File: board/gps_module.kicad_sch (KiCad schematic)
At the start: 0 parts

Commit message: Hopefully finished schema for pcb
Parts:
- added C11: 8.2p, symbol Device:C
- added C12, C9: 100n, symbol Device:C
- added C13: 4.7p, symbol Device:C
- added D4: LED, symbol Device:LED
- added J1: Conn_01x01_Pin, symbol Connector:Conn_01x01_Pin
- added L2, L3: 27n, symbol Device:L
- added R23: 10, symbol Device:R
- added R26: 470, symbol Device:R
- added TVS1: SMAJ30CA, Diode_SMD:D_SMA, symbol Diode:SMAJ30CA
- added U6: NEO-M7N, RF_GPS:ublox_NEO, symbol RF_GPS:NEO-M8N
- added U7: MAX2679B, Package_BGA:WLP-4_0.83x0.83mm_P0.4mm, symbol RF_Amplifier:MAX2679B
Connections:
- new net: C13.2, J1.1 (Pin_1), TVS1.2 (A2)
- new net: C13.1, L3.2
- new net: C11.2, U7.A2
- new net: D4.1 (K), R26.2
- new net: L3.1, U7.B1
- new net: L2.1, R23.2
- new net: R26.1, U6.3 (TIMEPULSE)
- new net +3V3: C12.2, C9.2, D4.2 (A), U6.23 (VCC), U7.A1 (Vcc)
- new net 3V3: U6.2 (D_SEL)
- new net GND: C12.1, C9.1, TVS1.1 (A1), U6.10 (GND), U6.12 (GND), U6.13 (GND), U6.24 (GND), U7.B2 (G)
- new net RF_IN: C11.1, L2.2, U6.11 (RF_IN)
- new net RX: U6.21 (RXD/SPI_MOSI)
- new net SDA_GPS: U6.18 (SDA/~{SPI_CS})
- new net SLC_GPS: U6.19 (SCL/SPI_CLK)
- new net TX: U6.20 (TXD/SPI_MISO)
- new net VCC_RF: R23.1, U6.8 (~{RESET}), U6.9 (VCC_RF)
- no-connect marks 0 -> 7
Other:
- note added: "GPS signal amplification"
- note added: "uBlox NEO M7N module"

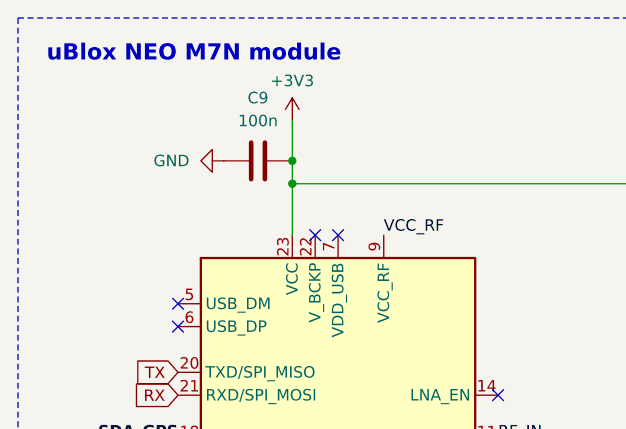
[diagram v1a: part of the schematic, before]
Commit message: Minor changes in shchema for PCB
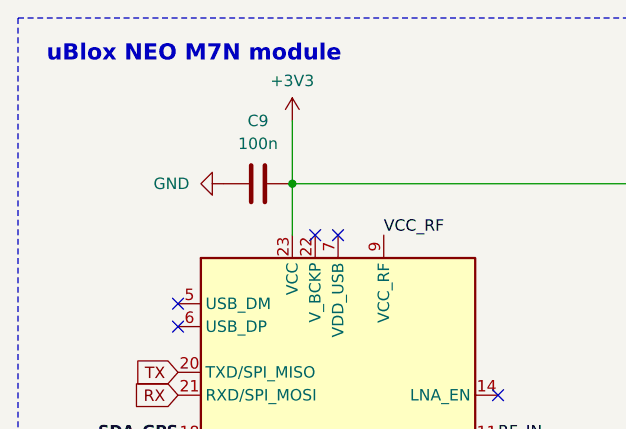
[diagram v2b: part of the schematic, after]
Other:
- moved on the sheet: C9
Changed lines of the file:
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@@
 (kicad_sch (version 20230121) (generator eeschema)
   (paper "A4")
-  (junction (at 94.615 73.66) (diameter 0) (color 0 0 0 0)
-  )
   (junction (at 221.615 95.885) (diameter 0) (color 0 0 0 0)
   )
@@
     (stroke (width 0) (type default))
   )
-  (wire (pts (xy 94.615 73.66) (xy 94.615 76.2))
-    (stroke (width 0) (type default))
-  )
   (wire (pts (xy 221.615 95.885) (xy 224.79 95.885))
     (stroke (width 0) (type default))
@@
     (stroke (width 0) (type default))
   )
-  (wire (pts (xy 94.615 69.215) (xy 94.615 73.66))
+  (wire (pts (xy 94.615 69.215) (xy 94.615 76.2))
     (stroke (width 0) (type default))
   )
@@
     )
   )
-  (symbol (lib_id "power:GND") (at 86.995 73.66 270) (unit 1)
-    (in_bom yes) (on_board yes) (dnp no) (fields_autoplaced)
-    (property "Reference" "#PWR041" (at 80.645 73.66 0)
-      (effects (font (size 1.27 1.27)) hide)
-    )
-    (property "Value" "GND" (at 83.185 73.66 90)
+  (symbol (lib_id "power:GND") (at 86.995 76.2 270) (unit 1)
+    (in_bom yes) (on_board yes) (dnp no) (fields_autoplaced)
+    (property "Reference" "#PWR041" (at 80.645 76.2 0)
+      (effects (font (size 1.27 1.27)) hide)
+    )
+    (property "Value" "GND" (at 83.185 76.2 90)
       (effects (font (size 1.27 1.27)) (justify right))
     )
-    (property "Footprint" "" (at 86.995 73.66 0)
-      (effects (font (size 1.27 1.27)) hide)
-    )
-    (property "Datasheet" "" (at 86.995 73.66 0)
+    (property "Footprint" "" (at 86.995 76.2 0)
+      (effects (font (size 1.27 1.27)) hide)
+    )
+    (property "Datasheet" "" (at 86.995 76.2 0)
       (effects (font (size 1.27 1.27)) hide)
     )
@@
     )
   )
-  (symbol (lib_id "Device:C") (at 90.805 73.66 90) (unit 1)
-    (in_bom yes) (on_board yes) (dnp no) (fields_autoplaced)
-    (property "Reference" "C9" (at 90.805 66.675 90)
-      (effects (font (size 1.27 1.27)))
-    )
-    (property "Value" "100n" (at 90.805 69.215 90)
-      (effects (font (size 1.27 1.27)))
-    )
-    (property "Footprint" "" (at 94.615 72.6948 0)
-      (effects (font (size 1.27 1.27)) hide)
-    )
-    (property "Datasheet" "~" (at 90.805 73.66 0)
-      (effects (font (size 1.27 1.27)) hide)
-    )
+  (symbol (lib_id "Device:C") (at 90.805 76.2 90) (unit 1)
+    (in_bom yes) (on_board yes) (dnp no) (fields_autoplaced)
+    (property "Reference" "C9" (at 90.805 69.215 90)
+      (effects (font (size 1.27 1.27)))
+    )
+    (property "Value" "100n" (at 90.805 71.755 90)
+      (effects (font (size 1.27 1.27)))
+    )
+    (property "Footprint" "" (at 94.615 75.2348 0)
+      (effects (font (size 1.27 1.27)) hide)
+    )
+    (property "Datasheet" "~" (at 90.805 76.2 0)
+      (effects (font (size 1.27 1.27)) hide)
+    )

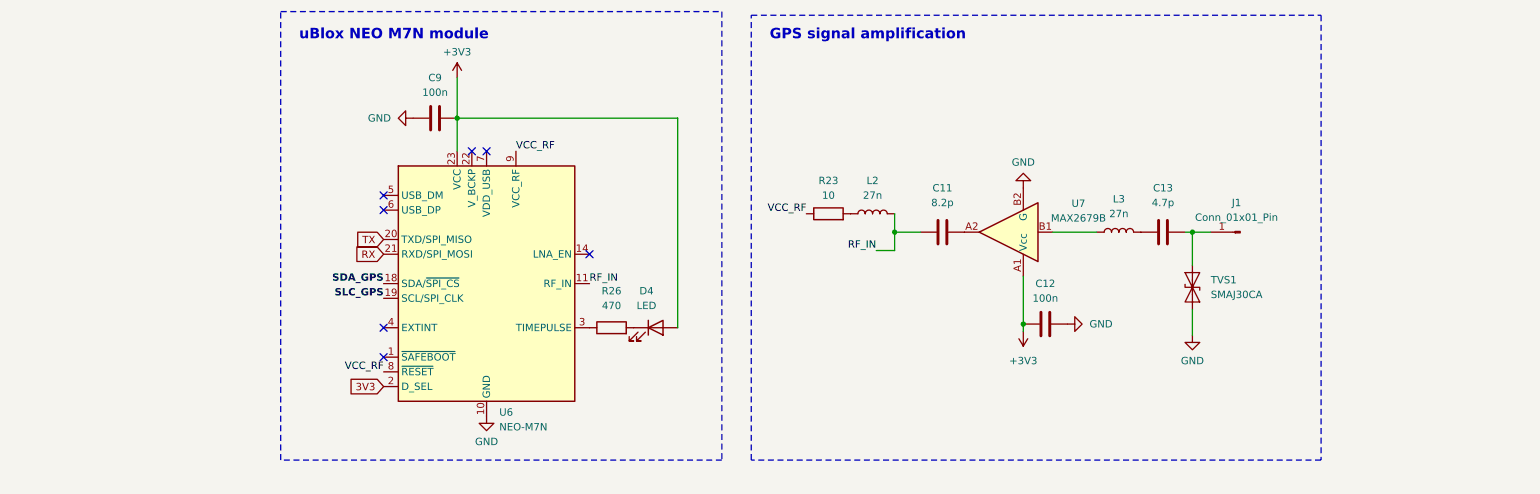
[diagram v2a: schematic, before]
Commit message: Updated schme to comply with electrical rules checker, prepared sensor logic for rewrite
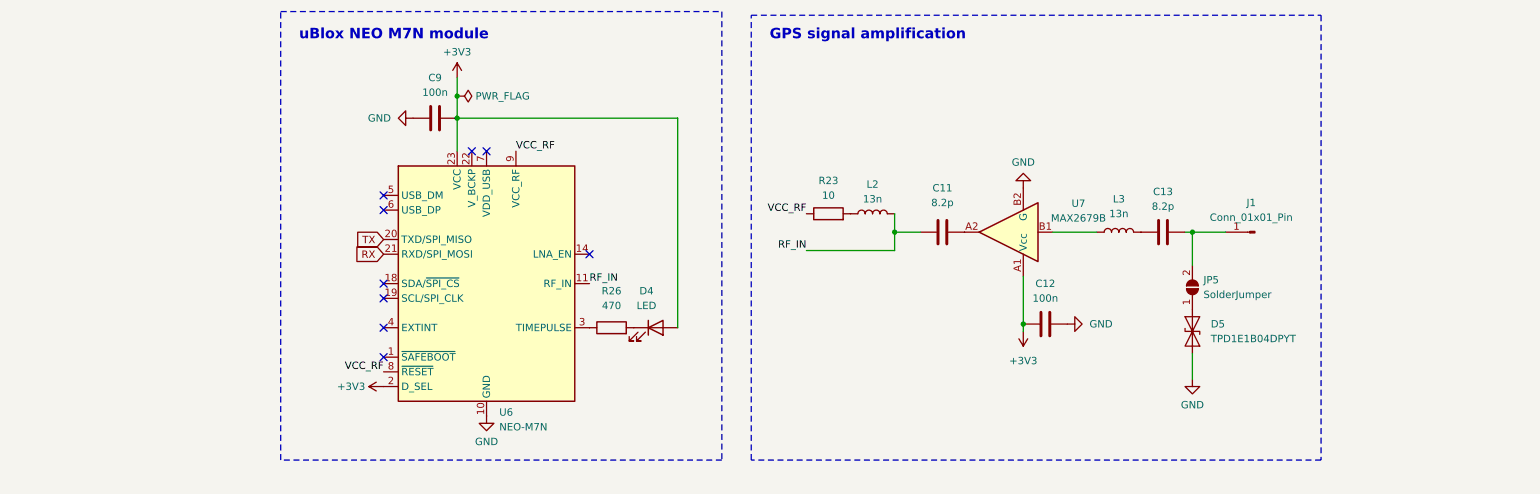
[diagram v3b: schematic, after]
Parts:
- removed TVS1: SMAJ30CA, Diode_SMD:D_SMA, symbol Diode:SMAJ30CA
- added D5: TPD1E1B04DPYT, Imported_Footprints:DPY_R-PX1SON-N2_, symbol Imported_Symbols:TPD1E1B04DPYT
- added JP5: SolderJumper, Jumper:SolderJumper-2_P1.3mm_Open_Pad1.0x1.5mm, symbol Jumper:SolderJumper_2_Open
- C11: footprint (none) -> Capacitor_SMD:C_0402_1005Metric
- C12, C9: footprint (none) -> Capacitor_SMD:C_0603_1608Metric
- C13: value 4.7p -> 8.2p; footprint (none) -> Capacitor_SMD:C_0402_1005Metric
- L2, L3: value 27n -> 13n; footprint (none) -> Inductor_SMD:L_0402_1005Metric
- R23, R26: footprint (none) -> Resistor_SMD:R_0603_1608Metric
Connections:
- net 3V3 is gone; now on net +3V3: U6.2 (D_SEL)
- net GND: now also D5.
- net at C13.2, J1.1 (Pin_1): now also JP5.2 (B)
- net SDA_GPS: no longer names the net of U6.18 (SDA/~{SPI_CS})
- net SLC_GPS: no longer names the net of U6.19 (SCL/SPI_CLK)
- new net: D5., JP5.1 (A)
- no-connect marks 7 -> 9
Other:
- title: (none) -> GPS Module
- moved on the sheet: J1

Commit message: More work in reformating drone side of codebase to be semi usable
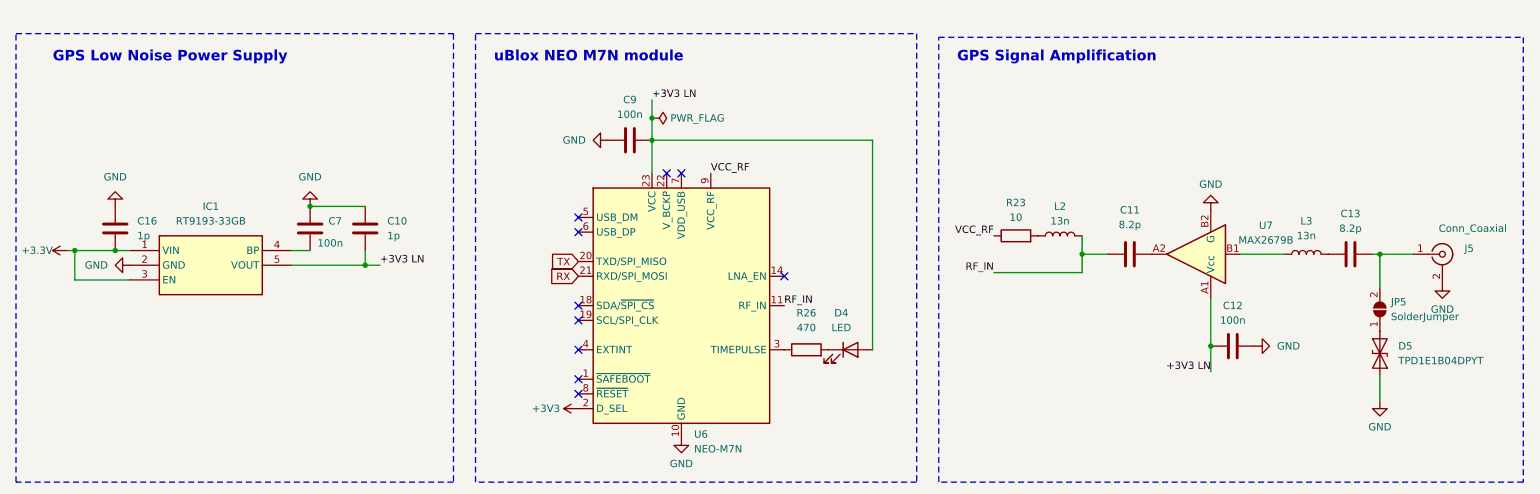
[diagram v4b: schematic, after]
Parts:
- removed J1: Conn_01x01_Pin, symbol Connector:Conn_01x01_Pin
- added C10, C16: 1p, Capacitor_SMD:C_0603_1608Metric, symbol Device:C
- added C7: 100n, Capacitor_SMD:C_0603_1608Metric, symbol Device:C
- added IC1: RT9193-33GB, Package_TO_SOT_SMD:SOT-23-5, symbol Imported_Symbols:RT9193-33GB
- added J5: Conn_Coaxial, Connector_Coaxial:U.FL_Molex_MCRF_73412-0110_Vertical, symbol Connector:Conn_Coaxial
- C11, C13: footprint Capacitor_SMD:C_0402_1005Metric -> Capacitor_SMD:C_0603_1608Metric
- D4: footprint (none) -> LED_SMD:LED_0805_2012Metric
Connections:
- net +3V3: no longer C12.2, C9.2, D4.2 (A), U6.23 (VCC), U7.A1 (Vcc)
- net GND: now also C10.1, C16.1, C7.1, IC1.2 (GND), J5.2 (Ext)
- net VCC_RF: no longer U6.8 (~{RESET})
- net at C13.2, JP5.2 (B): now also J5.1 (In)
- new net: C7.2, IC1.4 (BP)
- new net +3.3V: C16.2, IC1.1 (VIN), IC1.3 (EN)
- new net +3V3 LN: C10.2, C12.2, C9.2, D4.2 (A), IC1.5 (VOUT), U6.23 (VCC), U7.A1 (Vcc)
- no-connect marks 9 -> 10
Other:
- note added: "GPS Low Noise Power Supply"
- note added: "GPS Signal Amplification"
- note removed: "GPS signal amplification"
- moved on the sheet: C11, C12, C13, C9, D4, D5, JP5, L2, L3, R23, R26, U6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

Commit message: Started work on PCB design, more work on rewritting firmware to be semi usable
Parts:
- removed C13: 8.2p, Capacitor_SMD:C_0603_1608Metric, symbol Device:C
- removed D5: TPD1E1B04DPYT, Imported_Footprints:DPY_R-PX1SON-N2_, symbol Imported_Symbols:TPD1E1B04DPYT
- removed JP5: SolderJumper, Jumper:SolderJumper-2_P1.3mm_Open_Pad1.0x1.5mm, symbol Jumper:SolderJumper_2_Open
- removed U7: MAX2679B, Package_BGA:WLP-4_0.83x0.83mm_P0.4mm, symbol RF_Amplifier:MAX2679B
- added IC2: NJG1130KA1-TE1, Imported_Footprints:SOTFL50P160X60-6N, symbol Imported_Symbols:NJG1130KA1-TE1
- added L4: 18n, Inductor_SMD:L_0805_2012Metric, symbol Device:L
- added L5: 47n, Inductor_SMD:L_0603_1608Metric, symbol Device:L
- C11: value 8.2p -> 100n
- C12: value 100n -> 100p
- L2, L3: value 13n -> 8.7n; footprint Inductor_SMD:L_0402_1005Metric -> Inductor_SMD:L_0603_1608Metric
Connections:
- net +3V3 LN: now also C11.1, L2.1, L5.1; no longer C12.2
- net GND: now also C11.2, IC2.5 (GND_2), IC2.6 (GND_3), L4.2; no longer C12.1
- net RF_IN: now also C12.1, U6.9 (VCC_RF); no longer C11.1, L2.2
- net at L3.2: now also J5.1 (In)
- net at L3.1: now also IC2.4 (RF_IN), L4.1
- net at R23.2: now also IC2.1 (RF_OUT); no longer L2.1
- net VCC_RF: no longer names the net of R23.1
- net VCC_RF: now also C12.2, L5.2; no longer U6.9 (VCC_RF)
- new net: IC2.3 (VDD), L2.2
- no-connect marks 10 -> 11
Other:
- moved on the sheet: J5, L3

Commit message: First version of PCB finished
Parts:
- removed C9: 100n, Capacitor_SMD:C_0603_1608Metric, symbol Device:C
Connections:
- net +3.3V is gone; now on net +3V3: C16.2, IC1.1 (VIN), IC1.3 (EN)
- net +3V3: no longer U6.2 (D_SEL)
- net +3V3 LN: now also R26.2, U6.2 (D_SEL); no longer D4.2 (A)
- net GND: now also IC2.2 (GND_1)
- net at D4.1 (K): now also U6.3 (TIMEPULSE); no longer R26.2
- net at R26.1: now also D4.2 (A); no longer U6.3 (TIMEPULSE)
- no-connect marks 11 -> 10
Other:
- moved on the sheet: D4, R26

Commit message: Minor improvement to the board
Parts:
- added L6: 18n, Inductor_SMD:L_0805_2012Metric, symbol Device:L
- added R27: 10, Resistor_SMD:R_0603_1608Metric, symbol Device:R
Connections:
- net GND: now also L4.1; no longer L4.2
- net RF_IN: now also L6.2; no longer U6.9 (VCC_RF)
- net at IC2.4 (RF_IN), L3.1: now also L4.2; no longer L4.1
- new net: L6.1, R27.1
- new net VCC_RF: R27.2, U6.9 (VCC_RF)
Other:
- moved on the sheet: L4
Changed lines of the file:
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@@
     (rev "1.0")
   )
+  (junction (at 199.39 100.33) (diameter 0) (color 0 0 0 0)
+  )
+  (junction (at 199.39 109.22) (diameter 0) (color 0 0 0 0)
+  )
+  (junction (at 78.74 101.6) (diameter 0) (color 0 0 0 0)
+  )
+  (junction (at 250.825 100.33) (diameter 0) (color 0 0 0 0)
+  )
+  (junction (at 128.27 76.2) (diameter 0) (color 0 0 0 0)
+  )
+  (junction (at 27.94 99.06) (diameter 0) (color 0 0 0 0)
+  )
   (junction (at 191.77 92.71) (diameter 0) (color 0 0 0 0)
-  )
-  (junction (at 199.39 100.33) (diameter 0) (color 0 0 0 0)
-  )
-  (junction (at 199.39 109.22) (diameter 0) (color 0 0 0 0)
-  )
-  (junction (at 78.74 101.6) (diameter 0) (color 0 0 0 0)
-  )
-  (junction (at 250.825 100.33) (diameter 0) (color 0 0 0 0)
-  )
-  (junction (at 128.27 76.2) (diameter 0) (color 0 0 0 0)
-  )
-  (junction (at 27.94 99.06) (diameter 0) (color 0 0 0 0)
   )
   (junction (at 69.215 91.44) (diameter 0) (color 0 0 0 0)
@@
   (no_connect (at 115.57 95.885))
   (no_connect (at 115.57 93.345))
-  (wire (pts (xy 188.595 92.71) (xy 191.77 92.71))
+  (wire (pts (xy 186.69 92.71) (xy 191.77 92.71))
+    (stroke (width 0) (type default))
+  )
+  (wire (pts (xy 191.77 92.71) (xy 191.77 100.33))
     (stroke (width 0) (type default))
   )
@@
     (stroke (width 0) (type default))
   )
-  (wire (pts (xy 191.77 92.71) (xy 191.77 100.33))
+  (wire (pts (xy 191.77 81.915) (xy 191.77 83.82))
     (stroke (width 0) (type default))
   )
@@
     (stroke (width 0) (type default))
   )
-  (wire (pts (xy 191.77 86.36) (xy 188.595 86.36))
+  (wire (pts (xy 186.69 74.295) (xy 191.77 74.295))
     (stroke (width 0) (type default))
   )
@@
     (stroke (width 0) (type default))
   )
-  (wire (pts (xy 191.77 86.36) (xy 191.77 92.71))
+  (wire (pts (xy 191.77 91.44) (xy 191.77 92.71))
     (stroke (width 0) (type default))
   )
@@
     (effects (font (size 1.27 1.27)) (justify left bottom))
   )
-  (label "RF_IN" (at 188.595 92.71 180) (fields_autoplaced)
+  (label "RF_IN" (at 186.69 92.71 180) (fields_autoplaced)
     (effects (font (size 1.27 1.27)) (justify right bottom))
   )
@@
     (effects (font (size 1.27 1.27)) (justify left bottom))
   )
-  (label "VCC_RF" (at 188.595 86.36 180) (fields_autoplaced)
+  (label "VCC_RF" (at 186.69 74.295 180) (fields_autoplaced)
     (effects (font (size 1.27 1.27)) (justify right bottom))
   )
@@
     )
   )
+  (symbol (lib_id "Device:R") (at 191.77 78.105 180) (unit 1)
+    (in_bom yes) (on_board yes) (dnp no) (fields_autoplaced)
+    (property "Reference" "R27" (at 193.675 76.835 0)
+      (effects (font (size 1.27 1.27)) (justify right))
+    )
+    (property "Value" "10" (at 193.675 79.375 0)
+      (effects (font (size 1.27 1.27)) (justify right))
+    )
+    (property "Footprint" "Resistor_SMD:R_0603_1608Metric" (at 193.548 78.105 90)
+      (effects (font (size 1.27 1.27)) hide)
+    )
+    (property "Datasheet" "~" (at 191.77 78.105 0)
+      (effects (font (size 1.27 1.27)) hide)
+    )
+    (pin "1")
+    (pin "2")
+    (instances
+      (project "uav_project"
+        (path "/a8bf0924-b264-4c19-8c7e-9c0e131cacba/cca59cde-6ab1-4762-8541-6f874c4d6e1b"
+          (reference "R27") (unit 1)
+        )
+      )
+    )
+  )
   (symbol (lib_id "Device:C") (at 69.215 95.25 0) (unit 1)
     (in_bom yes) (on_board yes) (dnp no)
@@
     )
   )
-  (symbol (lib_id "Device:L") (at 250.825 95.885 180) (unit 1)
-    (in_bom yes) (on_board yes) (dnp no) (fields_autoplaced)
-    (property "Reference" "L4" (at 251.46 94.615 0)
-      (effects (font (size 1.27 1.27)) (justify right))
-    )
-    (property "Value" "18n" (at 251.46 97.155 0)
-      (effects (font (size 1.27 1.27)) (justify right))
+  (symbol (lib_id "Device:L") (at 250.825 95.885 0) (unit 1)
+    (in_bom yes) (on_board yes) (dnp no) (fields_autoplaced)
+    (property "Reference" "L4" (at 252.73 94.615 0)
+      (effects (font (size 1.27 1.27)) (justify left))
+    )
+    (property "Value" "18n" (at 252.73 97.155 0)
+      (effects (font (size 1.27 1.27)) (justify left))
     )
     (property "Footprint" "Inductor_SMD:L_0805_2012Metric" (at 250.825 95.885 0)
@@
         )
       )
+    )
+  )
+  (symbol (lib_id "Device:L") (at 191.77 87.63 0) (unit 1)
+    (in_bom yes) (on_board yes) (dnp no) (fields_autoplaced)
+    (property "Reference" "L6" (at 193.675 86.36 0)
+      (effects (font (size 1.27 1.27)) (justify left))
+    )
+    (property "Value" "18n" (at 193.675 88.9 0)
+      (effects (font (size 1.27 1.27)) (justify left))
+    )
+    (property "Footprint" "Inductor_SMD:L_0805_2012Metric" (at 191.77 87.63 0)
+      (effects (font (size 1.27 1.27)) hide)
+    )
+    (property "Datasheet" "~" (at 191.77 87.63 0)
+      (effects (font (size 1.27 1.27)) hide)
+    )
+    (pin "1")
+    (pin "2")
+    (instances
+      (project "uav_project"
+        (path "/a8bf0924-b264-4c19-8c7e-9c0e131cacba/cca59cde-6ab1-4762-8541-6f874c4d6e1b"
+          (reference "L6") (unit 1)
+        )
+      )
